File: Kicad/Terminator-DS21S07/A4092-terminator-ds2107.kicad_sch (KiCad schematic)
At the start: 8 parts, among them J1 Conn_02x25_Odd_Even, U1 DS21S07A, U2 DS21S07A

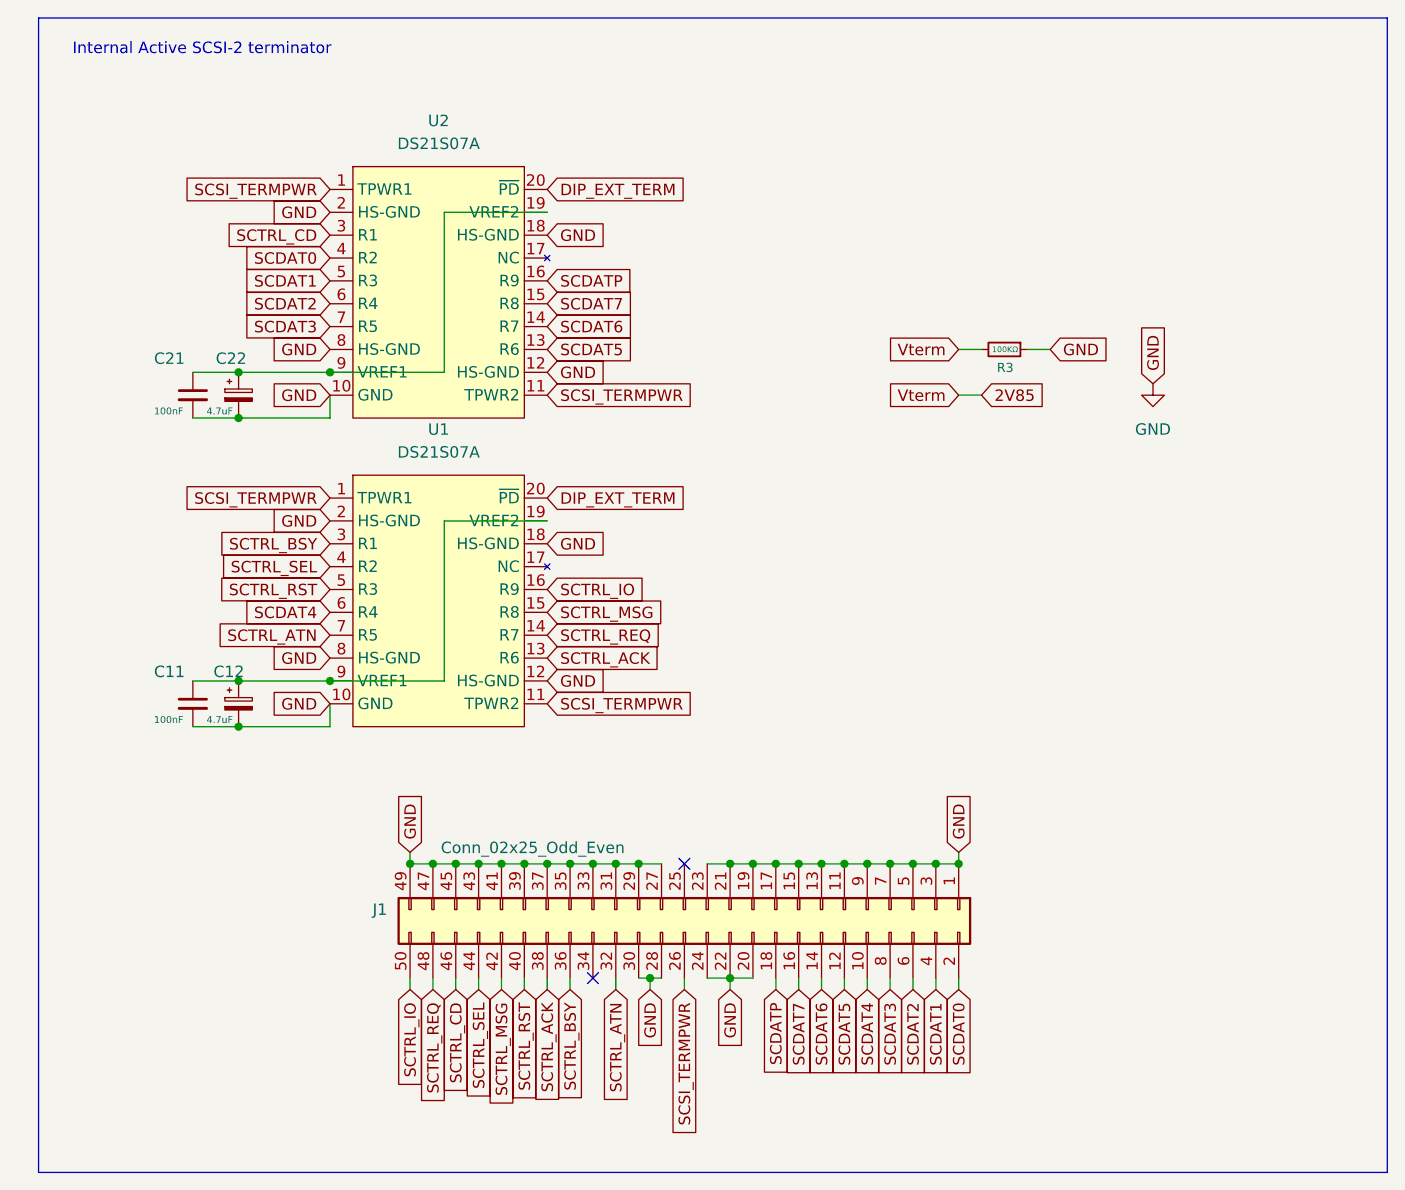
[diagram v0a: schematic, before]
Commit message: Finish DS2107 terminator
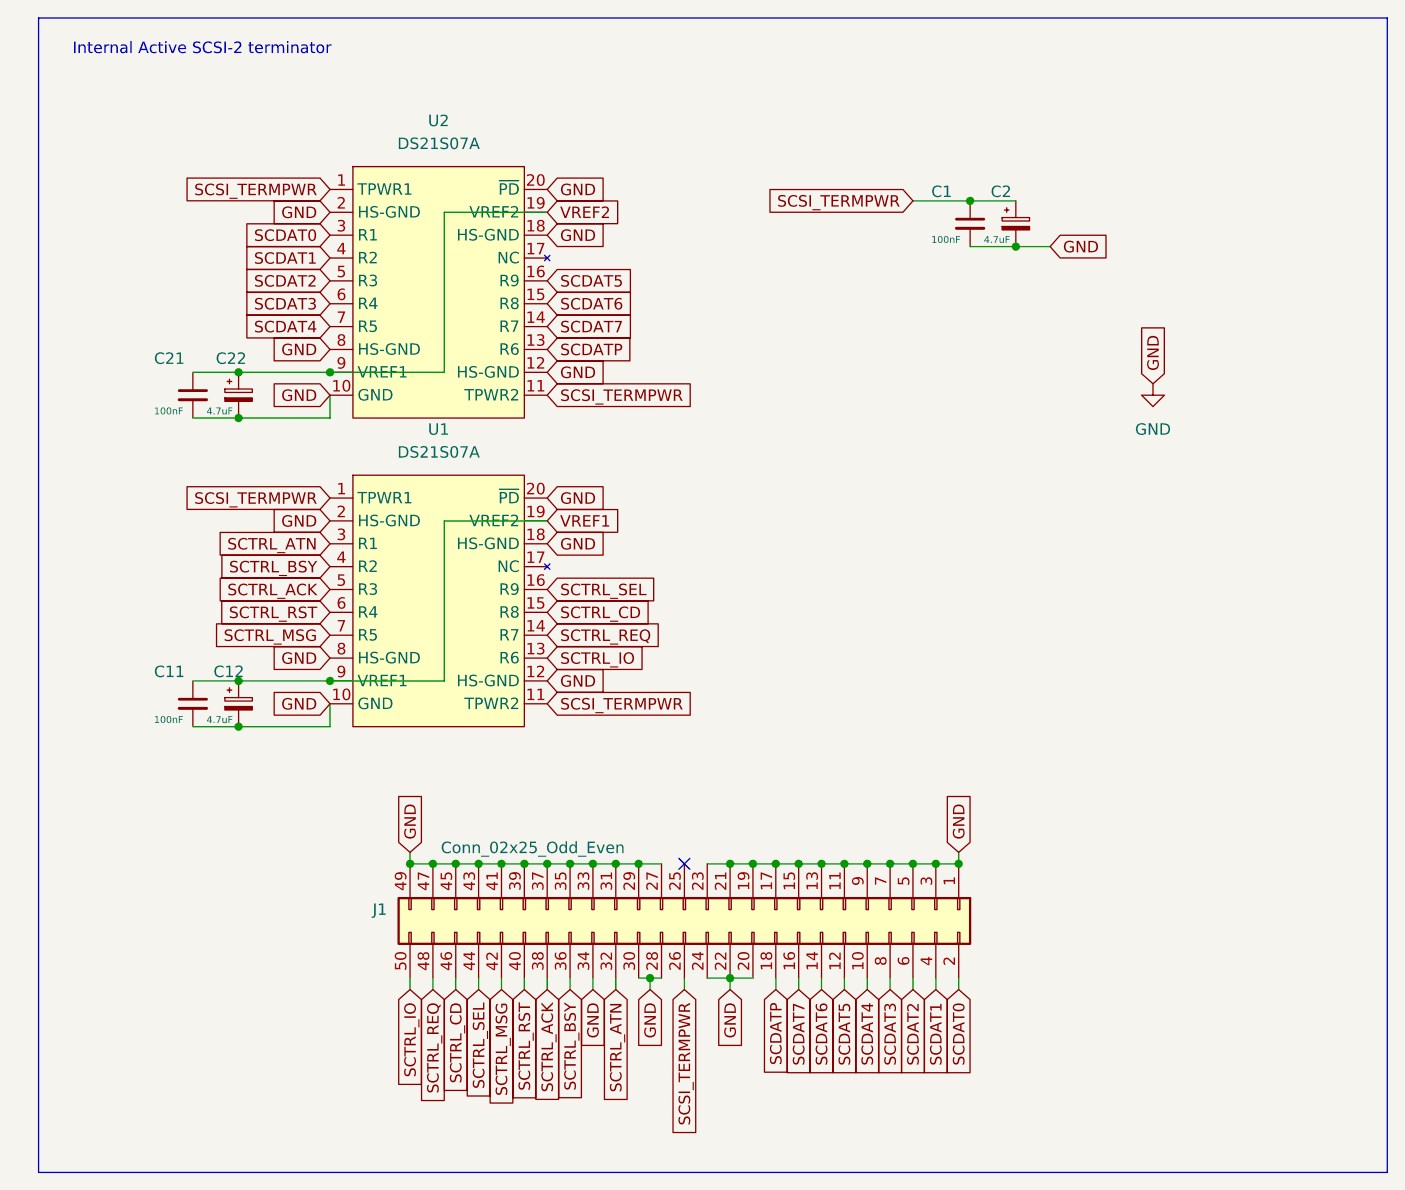
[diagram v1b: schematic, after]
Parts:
- removed R3: 100KΩ, Resistor_SMD:R_0603_1608Metric, symbol Device:R_Small
- added C1: 100nF, Capacitor_SMD:C_0603_1608Metric_Pad1.08x0.95mm_HandSolder, symbol Device:C_Small
- added C2: 4.7uF, Capacitor_Tantalum_SMD:CP_EIA-3216-10_Kemet-I_HandSolder, symbol Device:C_Polarized_Small
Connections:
- net DIP_EXT_TERM is gone; now on net GND: U1.20 (~{PD}), U2.20 (~{PD})
- net GND: now also J1.34 (Pin_34), C1.2, C2.2
- net SCDAT0: now also U2.3 (R1); no longer U2.4 (R2)
- net SCDAT1: now also U2.4 (R2); no longer U2.5 (R3)
- net SCDAT2: now also U2.5 (R3); no longer U2.6 (R4)
- net SCDAT3: now also U2.6 (R4); no longer U2.7 (R5)
- net SCDAT4: now also U2.7 (R5); no longer U1.6 (R4)
- net SCDAT5: now also U2.16 (R9); no longer U2.13 (R6)
- net SCDAT6: now also U2.15 (R8); no longer U2.14 (R7)
- net SCDAT7: now also U2.14 (R7); no longer U2.15 (R8)
- net SCDATP: now also U2.13 (R6); no longer U2.16 (R9)
- net SCSI_TERMPWR: now also C1.1, C2.1
- net SCTRL_ACK: now also U1.5 (R3); no longer U1.13 (R6)
- net SCTRL_ATN: now also U1.3 (R1); no longer U1.7 (R5)
- net SCTRL_BSY: now also U1.4 (R2); no longer U1.3 (R1)
- net SCTRL_CD: now also U1.15 (R8); no longer U2.3 (R1)
- net SCTRL_IO: now also U1.13 (R6); no longer U1.16 (R9)
- net SCTRL_MSG: now also U1.7 (R5); no longer U1.15 (R8)
- net SCTRL_RST: now also U1.6 (R4); no longer U1.5 (R3)
- net SCTRL_SEL: now also U1.16 (R9); no longer U1.4 (R2)
- net VREF1: now reaches C11.1, C12.1, U1.19 (VREF2), U1.9 (VREF1)
- net VREF2: now reaches C21.1, C22.1, U2.19 (VREF2), U2.9 (VREF1)
- no-connect marks 2 -> 1
